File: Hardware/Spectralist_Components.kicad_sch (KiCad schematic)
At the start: 103 parts, among them J1 Conn_01x08_Pin, J2 Conn_01x08_Pin, J3 Conn_01x10_Pin, J4 Conn_01x10_Pin, J5 Eurorack_10_pin_power, J6 SWD_Header, J7 UART_Test_Pins, J8 USB_B_Micro, U1 STM32H723VGTx, U2 PCM5100APW, U3 TPS561201, U4 LT1117-3.3, U5 MCP6004, U6 STF202-22T1G, U7 MCP6004, U8 TL072, Y1 8MHz 20pF

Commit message: Code tidy up; implementing CV , pots and trimmers
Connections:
- net Harm_Stretch_Pot: now also J3.8 (Pin_8), U1.33 (PC5); no longer J3.10 (Pin_10), U1.31 (PA7)
- net Harm_Warp_Pot: now also J3.10 (Pin_10), U1.31 (PA7); no longer J3.8 (Pin_8), U1.33 (PC5)
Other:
- note added: "v1.0 Errata: TPS561201 pads too long Harm_Warp_pot and Harm_Stretch_Pot wrong way round (fixed 1.1)"
- note removed: "v1.0 Errata: TPS561201 pads too long"
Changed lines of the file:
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@@
 		(title "Kishoof Components")
 		(date "2024-04-24")
-		(rev "1.0")
+		(rev "1.1")
 		(company "Mountjoy Modular")
 	)

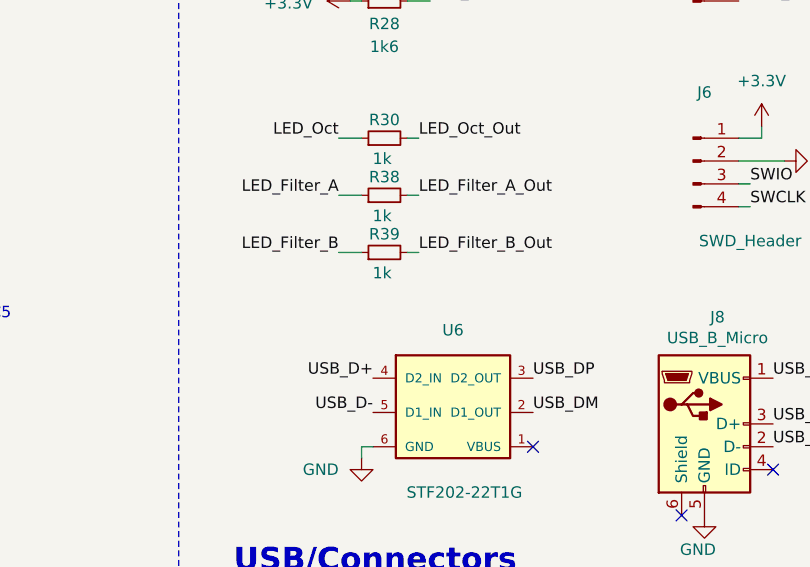
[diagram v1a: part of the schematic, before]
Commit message: Updated panel with correct sub-miniature switch hole size
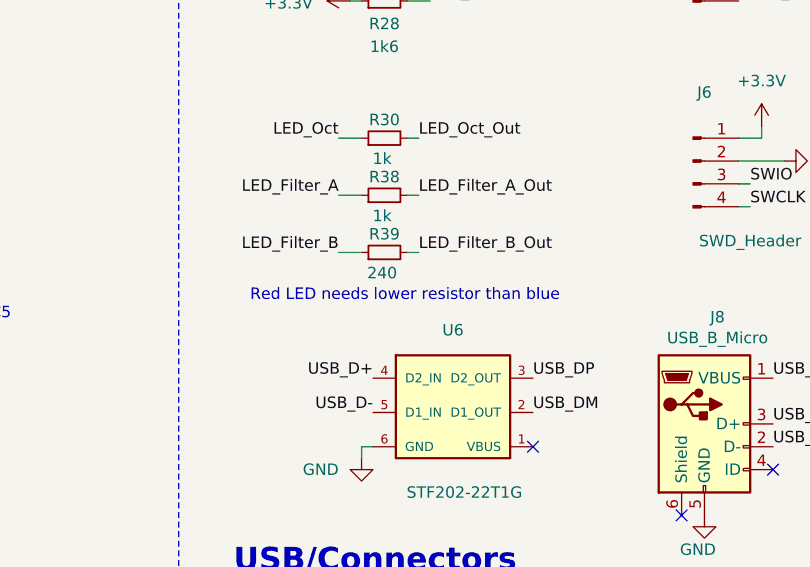
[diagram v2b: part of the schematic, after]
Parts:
- R39: value 1k -> 240
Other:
- note added: "Red LED needs lower resistor than blue"

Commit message: Code Clean up
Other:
- note added: "USART2"

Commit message: Added readme
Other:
- note added: "Gain: -47k/16k = -2.94 LP input cutoff: 1 / (2π * 1000 * 2.2e-9) = 72kHz LP Feedback filter cut off: 1 / 2πR_{f}C_{f} = 33.8KHz"
- note added: "v1.0 Errata: TPS561201 pads too long Harm_Warp_pot and Harm_Stretch_Pot wrong way round (fixed 1.1) Output RC LP filter unnecessary - can be done in op amp feedback"
- note removed: "Gain: -47k/16k = -2.94 Cutoff: 1 / (2π * 1000 * 2.2e-9) = 72kHz"
- note removed: "v1.0 Errata: TPS561201 pads too long Harm_Warp_pot and Harm_Stretch_Pot wrong way round (fixed 1.1)"
